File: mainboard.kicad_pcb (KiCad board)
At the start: 4 copper layers, 44.4 x 35.8 mm, 73 parts, among them J1 Conn_01x06, J2 USB_B_Micro, J3 xf2m-2415-1a, J4 XF2M-1015-1A, J5 Conn_01x02, J6 U.FL-R-SMT-1, J7 Conn_02x02_Top_Bottom, J8 Micro_SD_Card, SW1 KMR231NG LFS, U1 BMX160, U11 AP2112K-3.3, U2 MAX708RESA-T, U3 ATSAMD51J20A-M, U4 DRV8830DRC, U5 MR25H40, U6 DRV8830DRC, U8 DRV8830DRC, U9 RFM98PW-symbols, Y1 Crystal

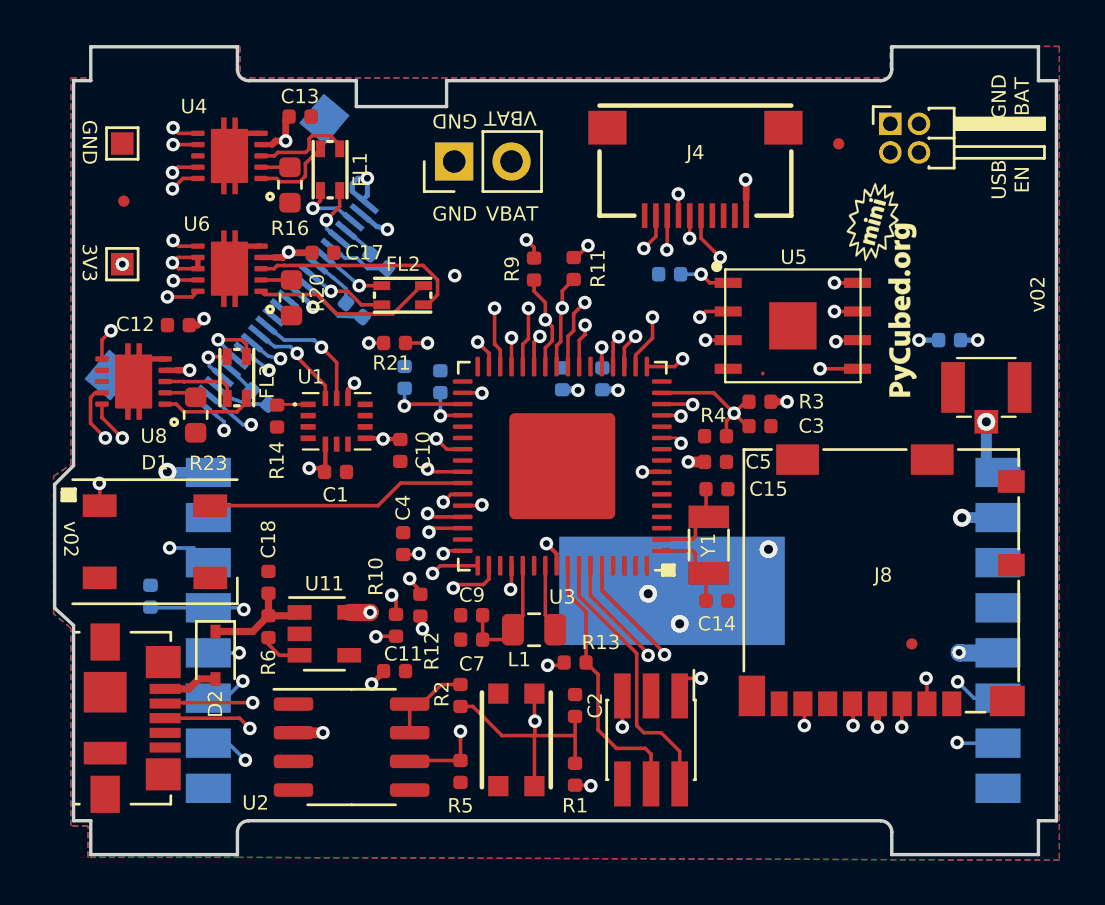
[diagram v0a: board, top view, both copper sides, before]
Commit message: Cleaned schematic, and moved components
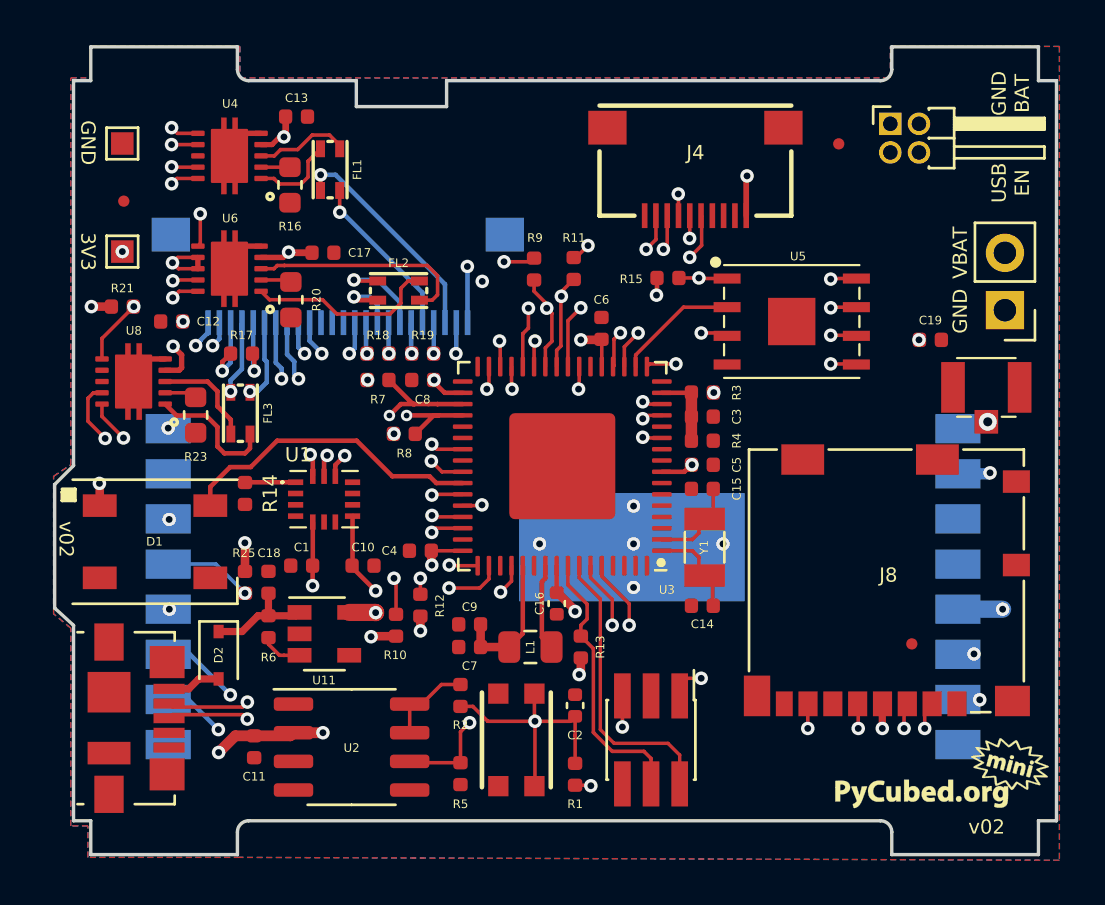
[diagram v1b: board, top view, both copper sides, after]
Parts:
- added C16: 0.1uF, Capacitor_SMD:C_0402_1005Metric, F.Cu at (98.8, 97.6)
- C19, R15, R17, R18, R19, R25, R7, R8: moved to F.Cu
- C6: value 1uF -> 0.1uF; moved to F.Cu
- C8: value 10uF -> 0.1uF; moved to F.Cu
- R21: value 10k -> 10K
- U2: value MAX708RESA-T -> MAX706RESA+
- moved J5 25.3 mm to (118.6, 84.6), turned to 180 degrees
- moved Ref** 21.6 mm to (115.8, 105.1), turned to 0 degrees
- moved R21 12.2 mm to (79.5, 84.4), turned to 0 degrees
- moved C11 7.07 mm to (85.3, 103.9), turned to -90 degrees
- moved Ref** 6.74 mm to (111.9, 79.8)
- moved C8 6.19 mm to (92.8, 87.7), turned to 180 degrees
- moved C10 5.37 mm to (90.2, 95.9), turned to 0 degrees
- moved R19 4.53 mm to (92.8, 86.5), turned to 0 degrees
- moved C1 4.42 mm to (87.4, 95.9), turned to 180 degrees
- moved R25 4.23 mm to (84.9, 96.6)
- moved R14 3.71 mm to (84.9, 92.7)
- moved U1 3.50 mm to (88.4, 93.0)
- moved R7 2.77 mm to (90.8, 87.7), turned to 180 degrees
- moved U9 2.63 mm to (98.9, 97.3)
- moved C3 2.59 mm to (105.2, 89.3)
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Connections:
- C2 pad 1: GND -> ~{RESET}
- C2 pad 2: ~RESET -> GND
- D1 pad 2: Net-(D1-Pad2) -> unconnected-(D1-Pad2)
- J1 pad 5: ~RESET -> ~{RESET}
- J1 pad 6: Net-(J1-Pad6) -> unconnected-(J1-Pad6)
- J2 pad 4: Net-(J2-Pad4) -> unconnected-(J2-Pad4)
- J3 pad 11: Net-(J3-Pad11) -> unconnected-(J3-Pad11)
- J4 pad 10: Net-(J4-Pad10) -> unconnected-(J4-Pad10)
- J4 pad 3: Net-(J4-Pad3) -> unconnected-(J4-Pad3)
- J8 pad 1: Net-(J8-Pad1) -> unconnected-(J8-Pad1)
- J8 pad 8: Net-(J8-Pad8) -> unconnected-(J8-Pad8)
- R1 pad 1: ~RESET -> ~{RESET}
- R2 pad 1: ~RESET -> ~{RESET}
- R7 pad 1: SDA2 -> SCL2
- R8 pad 1: SCL2 -> SDA2
- SW1 pad A: ~RESET -> ~{RESET}
- SW1 pad A': ~RESET -> ~{RESET}
- U1 pad 10: Net-(U1-Pad10) -> unconnected-(U1-Pad10)
- U1 pad 11: Net-(U1-Pad11) -> unconnected-(U1-Pad11)
- U1 pad 4: Net-(U1-Pad4) -> unconnected-(U1-Pad4)
- U1 pad 9: Net-(U1-Pad9) -> unconnected-(U1-Pad9)
- U11 pad 4: Net-(U11-Pad4) -> unconnected-(U11-Pad4)
- U2 pad 1: Net-(U2-Pad1) -> unconnected-(U2-Pad1)
- U2 pad 5: Net-(U2-Pad5) -> unconnected-(U2-Pad5)
- U3 pad 10: Net-(U3-Pad10) -> unconnected-(U3-Pad10)
- U3 pad 12: Net-(U3-Pad12) -> unconnected-(U3-Pad12)
- U3 pad 16: Net-(U3-Pad16) -> unconnected-(U3-Pad16)
- U3 pad 3: Net-(U3-Pad3) -> unconnected-(U3-Pad3)
- U3 pad 32: Net-(U3-Pad32) -> unconnected-(U3-Pad32)
- U3 pad 37: Net-(U3-Pad37) -> unconnected-(U3-Pad37)
- U3 pad 38: Net-(U3-Pad38) -> unconnected-(U3-Pad38)
- U3 pad 4: Net-(U3-Pad4) -> unconnected-(U3-Pad4)
- U3 pad 40: Net-(U3-Pad40) -> unconnected-(U3-Pad40)
- U3 pad 5: Net-(U3-Pad5) -> unconnected-(U3-Pad5)
- U3 pad 51: Net-(U3-Pad51) -> unconnected-(U3-Pad51)
- U3 pad 52: ~RESET -> ~{RESET}
- U3 pad 6: Net-(U3-Pad6) -> unconnected-(U3-Pad6)
- U3 pad 62: Net-(U3-Pad62) -> unconnected-(U3-Pad62)
- U3 pad 63: Net-(U3-Pad63) -> unconnected-(U3-Pad63)
- U3 pad 64: Net-(U3-Pad64) -> unconnected-(U3-Pad64)
- U3 pad 9: Net-(U3-Pad9) -> unconnected-(U3-Pad9)
- U9 pad 15: Net-(U9-Pad15) -> unconnected-(U9-Pad15)
- U9 pad 3: Net-(U9-Pad3) -> unconnected-(U9-Pad3)
- U9 pad 4: Net-(U9-Pad4) -> unconnected-(U9-Pad4)
- U9 pad 8: Net-(U9-Pad8) -> unconnected-(U9-Pad8)
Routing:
- net ~RESET: track 24.8 -> 0.00 mm, vias 3 -> 0
- net ~{RESET}: track 0.00 -> 24.7 mm, vias 0 -> 3
- net +3V3: track 26.9 -> 39.7 mm, vias 26 -> 28
- net BATT_P: track 91.4 -> 99.6 mm
- net COIL1_P: track 2.94 -> 9.92 mm
- net SCL3: track 53.1 -> 46.8 mm
- net M_FAULT: track 41.3 -> 36.1 mm, vias 5 -> 4
- net COIL2_N: track 2.65 -> 7.44 mm
- net SDA3: track 56.7 -> 52.0 mm
- net RF_IO0: track 25.0 -> 20.9 mm
- net GND: track 13.0 -> 9.26 mm, vias 10 -> 9
- net RF_IO1: track 25.6 -> 22.0 mm
- net SCL2: track 13.9 -> 17.4 mm
- net /BATTERY: track 6.50 -> 3.45 mm, vias 1 -> 0
- net SCL1: track 19.8 -> 22.8 mm, vias 2 -> 3
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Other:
- net class Default removed

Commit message: Made suggested changes
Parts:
- J4: value XF2M-1015-1A -> 2x5 Pin Header 1.27mm; footprint custom-footprints:XF2M-1015-1A -> Connector_PinHeader_1.27mm:PinHeader_2x05_P1.27mm_Vertical_SMD
- J6: moved to B.Cu
- moved J6 10.6 mm to (108.2, 83.7), turned to 180 degrees
- moved J4 5.36 mm to (100.0, 78.2), turned to 90 degrees
- moved J2 1.37 mm to (78.7, 102.7)
- moved D2 0.47 mm to (83.7, 99.4)
- moved R11 0.40 mm to (99.7, 83.1), turned to 0 degrees
- moved R9 0.34 mm to (97.7, 83.1), turned to 180 degrees
- renumbered R23 to R21, R21 to R22, R25 to R23, U11 to U7
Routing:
- net Net-(J6-Pad3): track 2.79 -> 14.9 mm, vias 1 -> 0
- net MOSI: track 76.7 -> 69.8 mm
- net BATT_P: track 99.6 -> 103.9 mm
- net MISO: track 72.0 -> 68.4 mm
- net GND: track 9.26 -> 12.2 mm, vias 9 -> 10
- net +3V3: track 39.7 -> 41.4 mm
- net USB_D-: track 17.4 -> 18.7 mm
- net USB_D+: track 18.3 -> 19.7 mm
- net VUSB: track 2.55 -> 3.89 mm
- net EN_CAM: track 19.8 -> 19.0 mm, vias 3 -> 2
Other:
- outline, holes or cut-outs redrawn

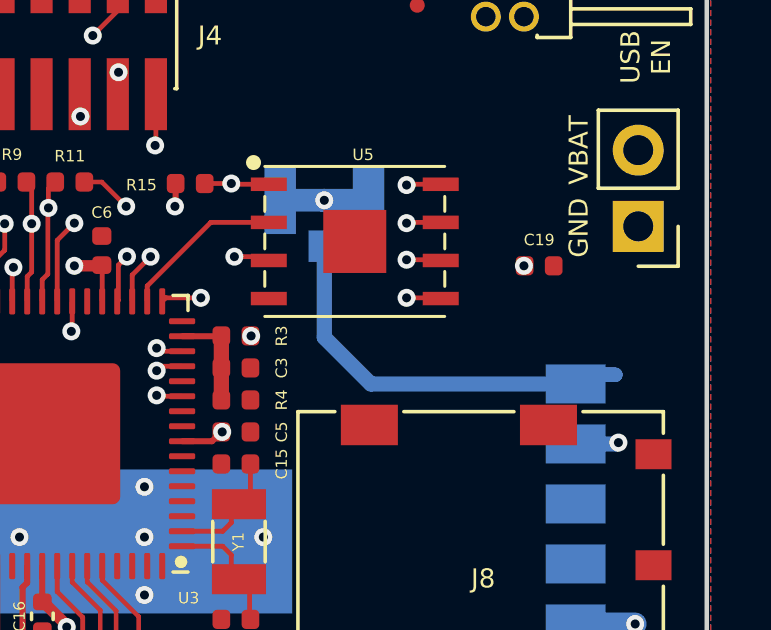
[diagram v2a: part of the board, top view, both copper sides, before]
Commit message: Curved radio trace
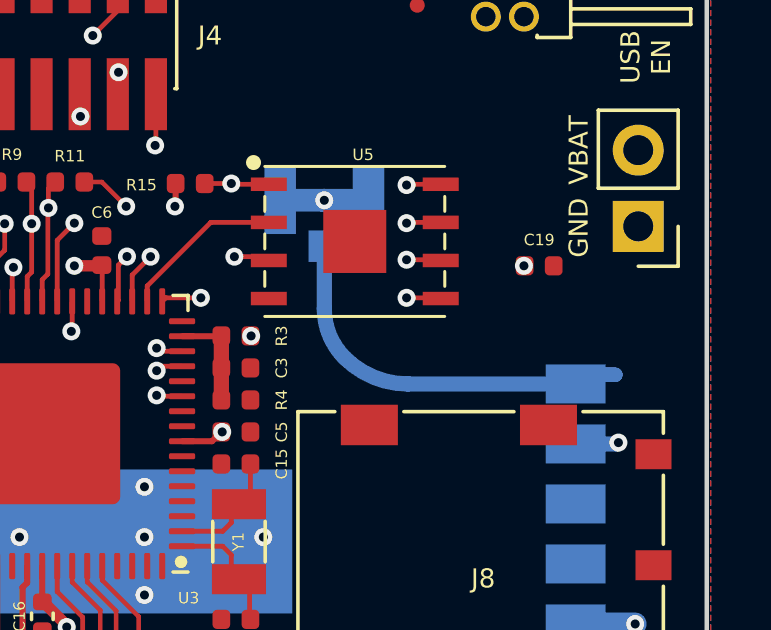
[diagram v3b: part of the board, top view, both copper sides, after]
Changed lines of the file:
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@@
   (segment (start 93.3024 86.5066) (end 93.2966 86.5124) (width 0.2032) (layer "B.Cu") (net 55))
   (segment (start 117.856 89.535) (end 116.839792 89.535) (width 0.48) (layer "B.Cu") (net 56))
-  (segment (start 108.1532 85.2434) (end 108.1532 88.2904) (width 0.508) (layer "B.Cu") (net 56))
+  (segment (start 108.1532 85.2434) (end 108.1532 87.331551) (width 0.508) (layer "B.Cu") (net 56))
   (segment (start 117.856 89.535) (end 116.8398 89.535) (width 0.48) (layer "B.Cu") (net 56))
-  (segment (start 109.703601 89.840801) (end 116.533991 89.840801) (width 0.508) (layer "B.Cu") (net 56))
+  (segment (start 110.937347 89.840801) (end 116.533991 89.840801) (width 0.508) (layer "B.Cu") (net 56))
   (segment (start 116.8398 89.535) (end 116.6108 89.764) (width 0.48) (layer "B.Cu") (net 56))
   (segment (start 116.839792 89.535) (end 116.533991 89.840801) (width 0.48) (layer "B.Cu") (net 56))
-  (segment (start 108.1532 88.2904) (end 109.703601 89.840801) (width 0.508) (layer "B.Cu") (net 56))
+  (arc (start 108.1532 87.331551) (mid 108.329408 88.217411) (end 108.831211 88.968411) (width 0.508) (layer "B.Cu") (net 56))
+  (arc (start 110.937347 89.840801) (mid 109.797514 89.614074) (end 108.831211 88.968411) (width 0.508) (layer "B.Cu") (net 56))
   (segment (start 92.237 102.0445) (end 92.7735 102.0445) (width 0.16) (layer "F.Cu") (net 57))
   (segment (start 92.7735 102.0445) (end 93.6395 101.1785) (width 0.16) (layer "F.Cu") (net 57))

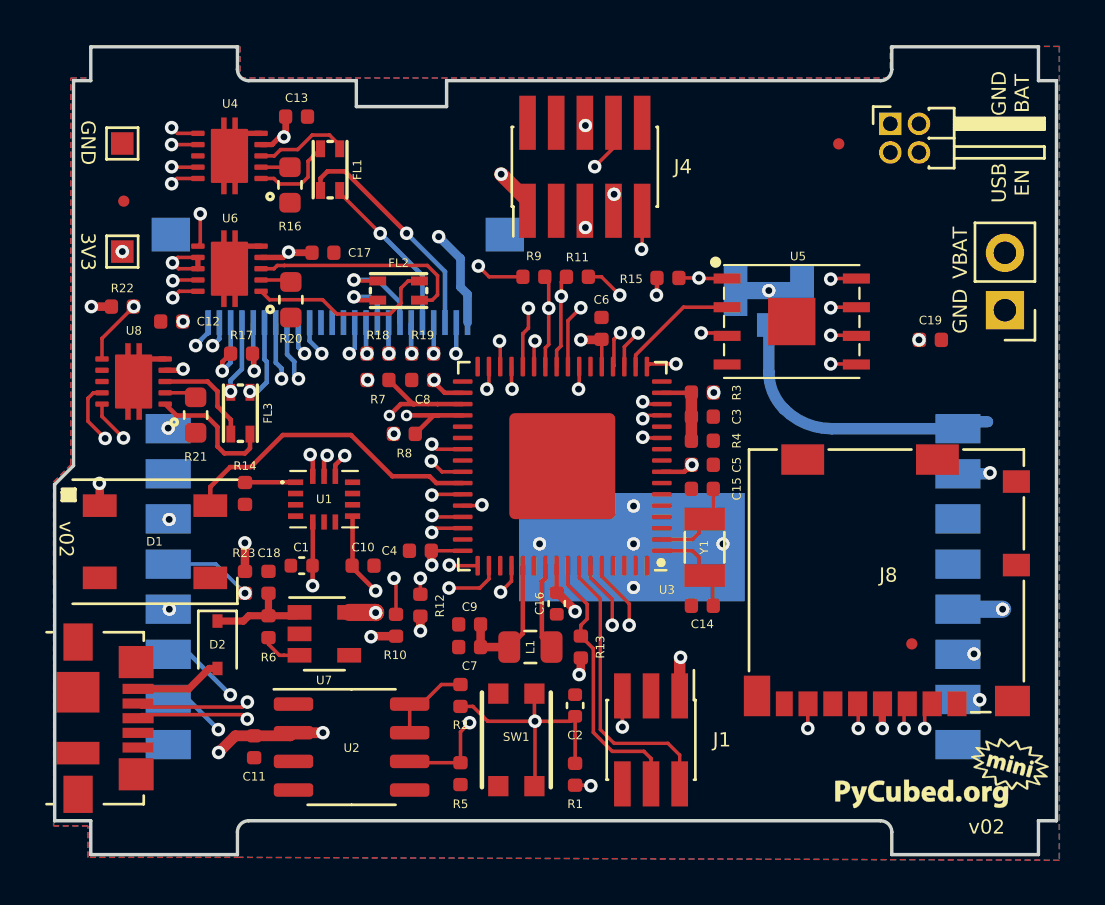
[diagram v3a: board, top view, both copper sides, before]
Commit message: Moved Rf Antenna. Change J7 to 1x5 Header
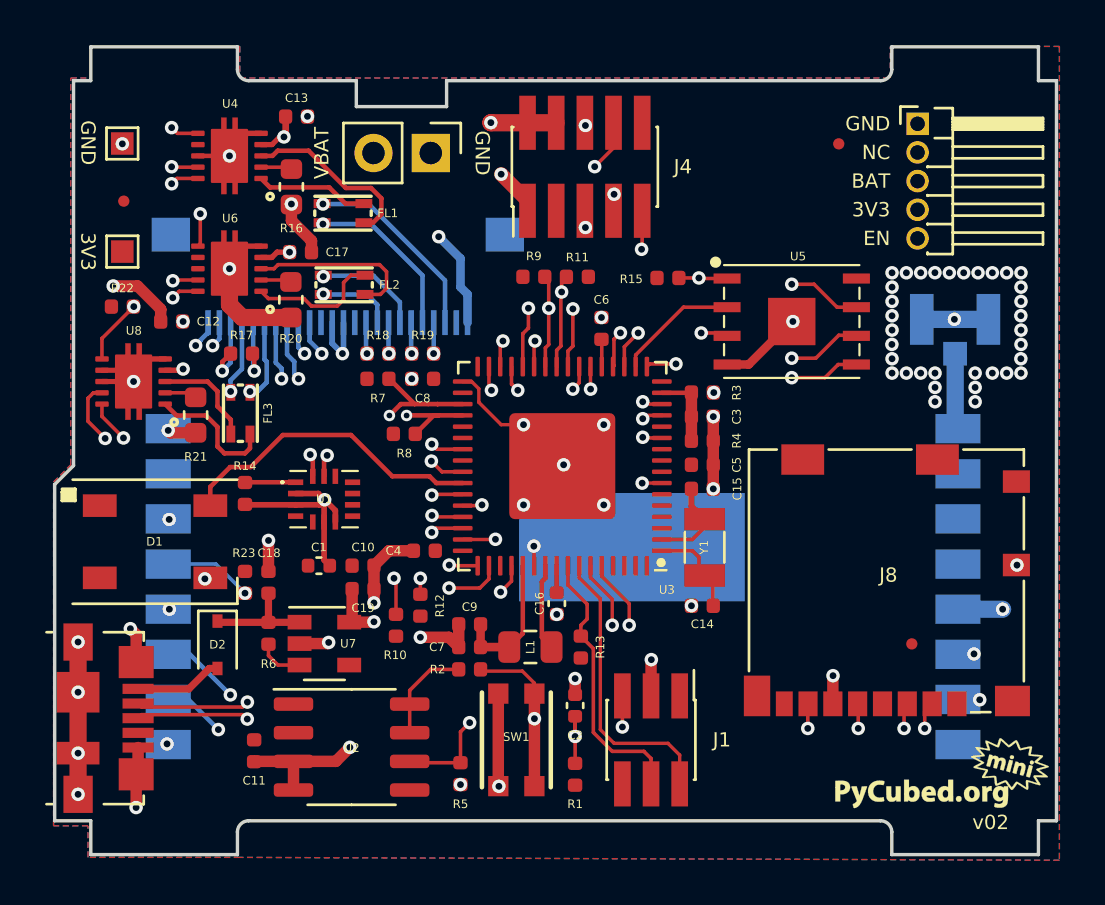
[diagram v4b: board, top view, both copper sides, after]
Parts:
- J7: value Conn_02x02_Top_Bottom -> Conn_01x05; footprint Connector_PinHeader_1.27mm:PinHeader_2x02_P1.27mm_Horizontal -> Connector_PinHeader_1.27mm:PinHeader_1x05_P1.27mm_Horizontal
- moved C19 27.5 mm to (90.2, 97.0)
- moved J5 26.4 mm to (93.2, 77.6), turned to -90 degrees
- moved J6 8.35 mm to (116.4, 85.0)
- moved FL2 2.43 mm to (89.3, 83.5)
- moved FL1 2.01 mm to (89.3, 80.3), turned to 180 degrees
- moved R2 1.23 mm to (94.9, 100.5), turned to 180 degrees
- moved J7 1.21 mm to (114.7, 76.3)
- moved C17 0.99 mm to (87.4, 82.0)
- moved C1 0.76 mm to (88.2, 95.9), turned to 0 degrees
- moved U7 0.43 mm to (88.5, 99.4)
- moved R6 0.29 mm to (86.0, 98.9)
- moved Ref** 0.25 mm to (111.9, 79.5)
- moved C4 0.18 mm to (92.9, 95.2)
- moved C11 0.18 mm to (85.3, 104.1)
- moved R16 0.10 mm to (87.0, 79.1)
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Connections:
- J7 pad 2: BATT_P -> unconnected-(J7-Pad2)
- J7 pad 3: +3V3 -> BATT_P
- J7 pad 4: Net-(C19-Pad1) -> +3V3
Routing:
- net GND: track 12.2 -> 87.0 mm, vias 10 -> 79
- net +3V3: track 41.4 -> 5.49 mm, vias 28 -> 2
- net Net-(J6-Pad3): track 14.6 -> 3.37 mm
- net BATT_P: track 103.9 -> 95.0 mm
- net Net-(FL1-Pad1): track 4.21 -> 7.94 mm
- net Net-(FL2-Pad3): track 8.43 -> 5.89 mm
- net Net-(FL2-Pad1): track 9.82 -> 7.57 mm
- net COIL1_P: track 10.3 -> 8.68 mm
- net Net-(FL1-Pad3): track 3.79 -> 5.02 mm
- net ~{RESET}: track 24.7 -> 23.5 mm, vias 3 -> 4
- net FLASH_IO3: track 12.6 -> 13.4 mm
- net SCK: track 65.8 -> 66.6 mm
- net FLASH_SCK: track 14.1 -> 14.9 mm
- net Net-(R2-Pad2): track 3.88 -> 4.43 mm
- net Net-(C19-Pad1): track 46.0 -> 45.7 mm, vias 2 -> 1
- added copper zone on F.Cu, net +3V3
- added copper zone on B.Cu, net GND
- added copper zone on In2.Cu, net GND
- removed copper zone on B.Cu, net +3V3
- removed copper zone on F.Cu, net GND
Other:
- board text added: "BAT"
- board text added: "EN"
- board text added: "NC"
- board text removed: "GND BAT"
- board text removed: "USB EN"
